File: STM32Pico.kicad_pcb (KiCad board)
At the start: 2 copper layers, 21.1 x 51.3 mm, 25 parts, among them J1 2.54mm header 01x20, J2 2.54mm header 01x20, SW1 Boot Mode, SW2 Reset Switch, U1 STM32F411CEUx, U2 XC6206PxxxMR, X1 ECS-2520MV-xxx-xx

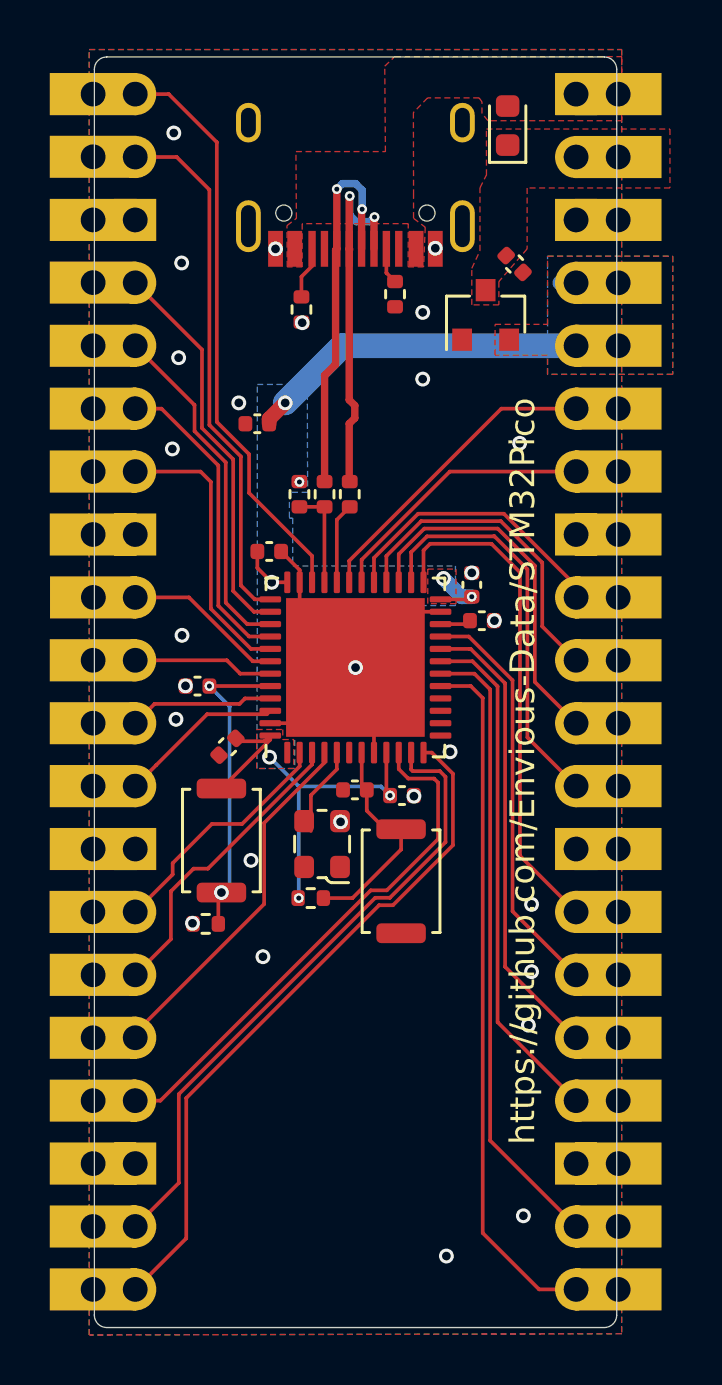
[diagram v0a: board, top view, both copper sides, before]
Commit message: added pin lables and Jtag/swdio/swclk on the PCB
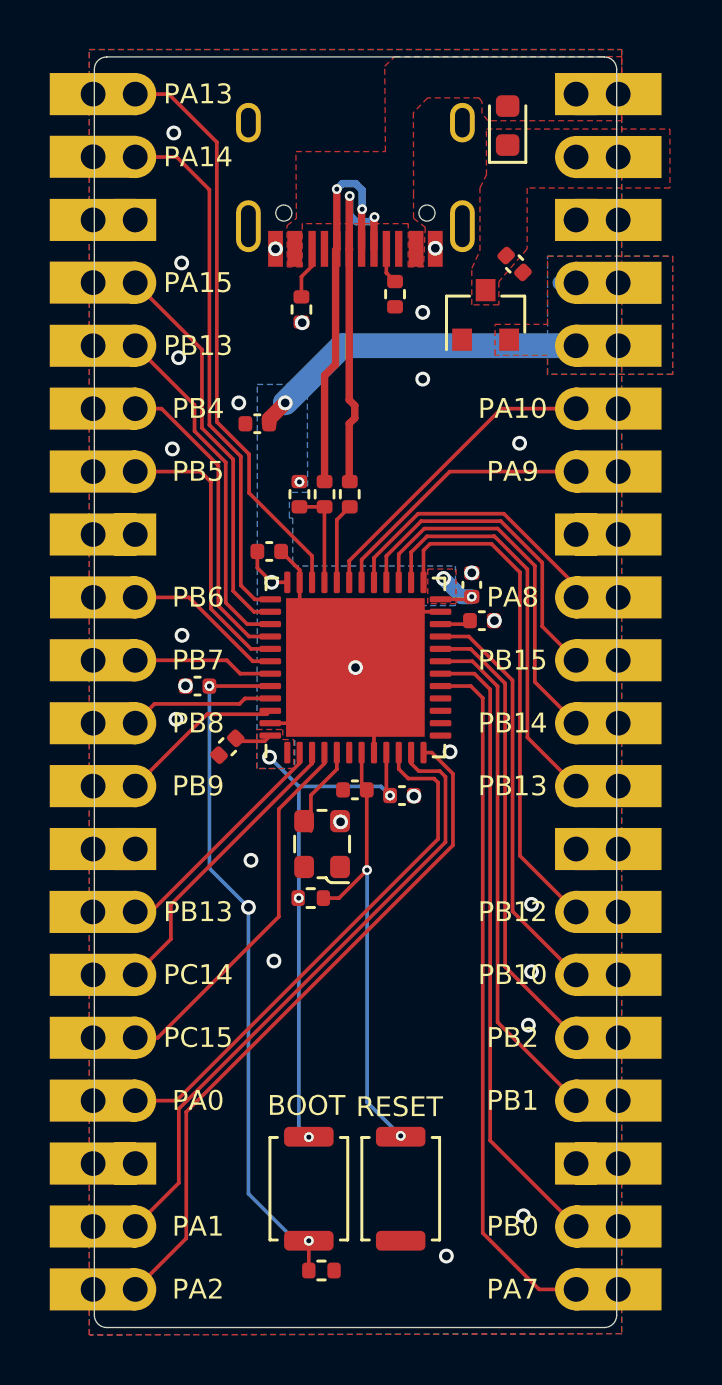
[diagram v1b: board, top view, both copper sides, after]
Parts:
- moved R7 14.8 mm to (102.3, 106.2), turned to 0 degrees
- moved SW1 14.5 mm to (101.8, 102.9)
- moved SW2 12.4 mm to (105.5, 102.9)
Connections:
- net PA13 renamed PA13-SWDIO
- net PA14 renamed PA14-SWCLK
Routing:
- net boot0: track 12.6 -> 28.0 mm, vias 2 -> 3
- net resetsw: track 8.91 -> 18.4 mm, vias 0 -> 2
- net +3V3: track 36.6 -> 43.4 mm, vias 8 -> 9
- net PC15: track 14.7 -> 15.2 mm
- net GND: vias 28 -> 27
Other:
- board text added: "BOOT"
- board text added: "JTCK"
- board text added: "JTDI"
- board text added: "JTMS"
- board text added: "PA0"
- board text added: "PA1"
- board text added: "PA10"
- board text added: "PA13"
- board text added: "PA14"
- board text added: "PA15"
- board text added: "PA2"
- board text added: "PA7"
- board text added: "PA8"
- board text added: "PA9"
- board text added: "PB0"
- board text added: "PB1"
- board text added: "PB10"
- board text added: "PB12"
- board text added: "PB13"
- board text added: "PB14"
- board text added: "PB15"
- board text added: "PB2"
- board text added: "PB4"
- board text added: "PB5"
- board text added: "PB6"
- board text added: "PB7"
- board text added: "PB8"
- board text added: "PB9"
- board text added: "PC14"
- board text added: "PC15"
- board text added: "RESET"
- board text added: "SWCLK"
- board text added: "SWDIO"
- board text removed: "https://github.com/Envious-Data/STM32Pico"

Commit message: changed diode for more common type
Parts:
- D1: value 1N4002 0603 -> 1N4002; footprint Diode_SMD:D_0603_1608Metric -> Diode_SMD:D_SOD-123

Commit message: adjusted pin labels
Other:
- board text added: "3V3"
- board text added: "VBUS"
- board text added: "VSYS"

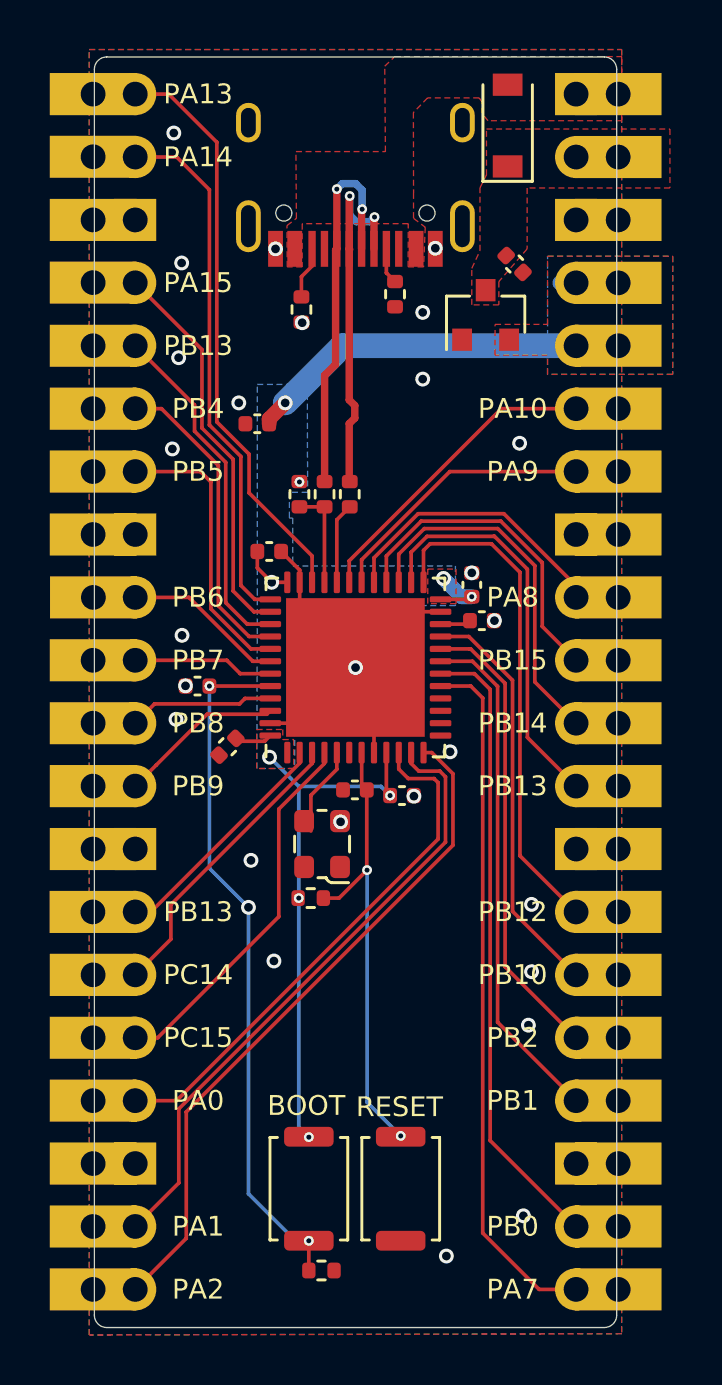
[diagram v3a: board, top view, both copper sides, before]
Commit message: swapped oscilator for crystal and adjusted various nearby parts and traces.
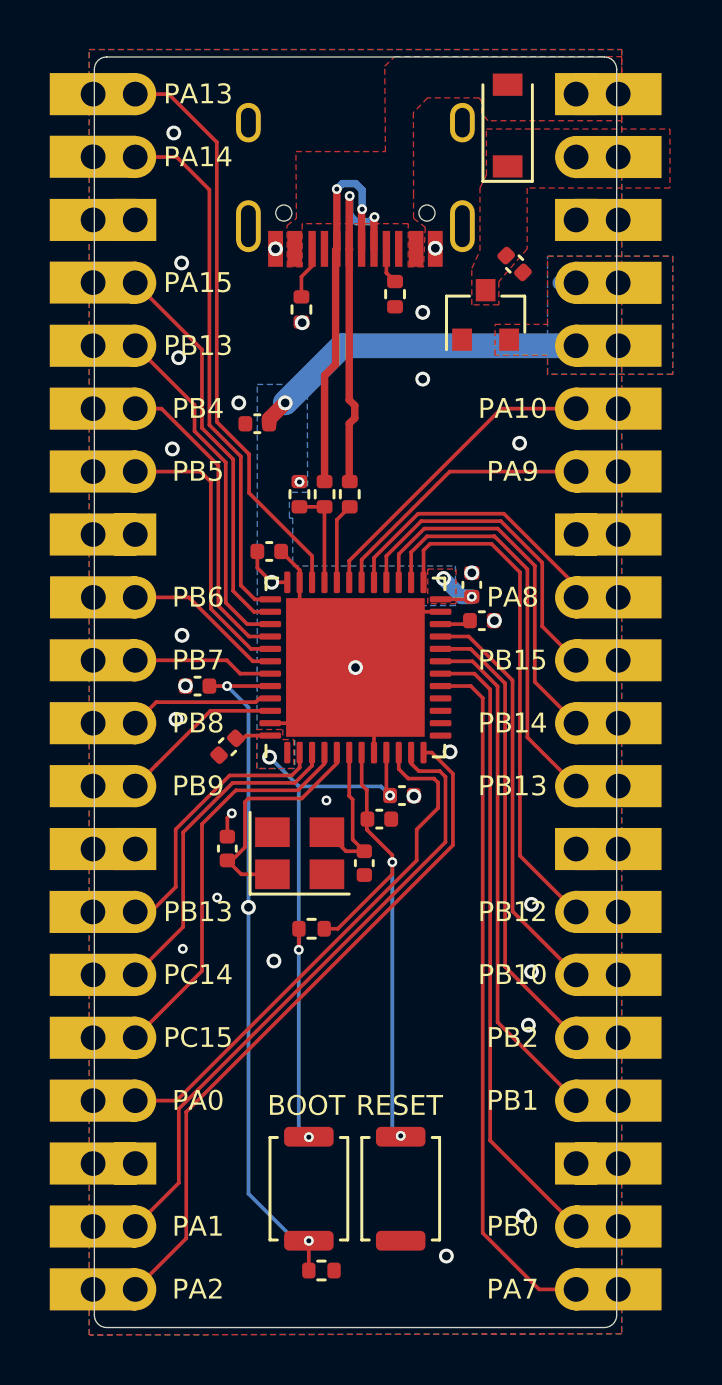
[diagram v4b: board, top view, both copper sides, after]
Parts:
- removed X1: ECS-2520MV-xxx-xx, Oscillator:Oscillator_SMD_ECS_2520MV-xxx-xx-4Pin_2.5x2.0mm
- added C10: 22pf capacitor, Capacitor_SMD:C_0402_1005Metric, F.Cu at (98.5, 89.2)
- added C11: 22pf capacitor, Capacitor_SMD:C_0402_1005Metric, F.Cu at (104.0, 89.8)
- added Y1: 8Mhz 3225, Crystal:Crystal_SMD_3225-4Pin_3.2x2.5mm, F.Cu at (101.4, 89.4)
- moved C9 1.54 mm to (104.6, 88.0), turned to 0 degrees
- moved R6 1.24 mm to (101.9, 92.4)
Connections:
- U1 pad 5: OSCpin -> OSCIN
- U1 pad 6: (no net) -> OSCOUT
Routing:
- net OSCIN: track 0.00 -> 9.60 mm
- net OSCOUT: track 0.00 -> 6.06 mm
- net OSCpin: track 3.60 -> 0.00 mm
- net resetsw: track 18.4 -> 20.3 mm
- net PC14: track 11.9 -> 13.4 mm
- net PC13: track 9.55 -> 11.0 mm
- net GND: track 18.4 -> 19.4 mm, vias 27 -> 29
- net PC15: track 15.2 -> 16.1 mm
- net +3V3: track 43.4 -> 44.3 mm

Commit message: added github url and fixed usb traces to not require vias
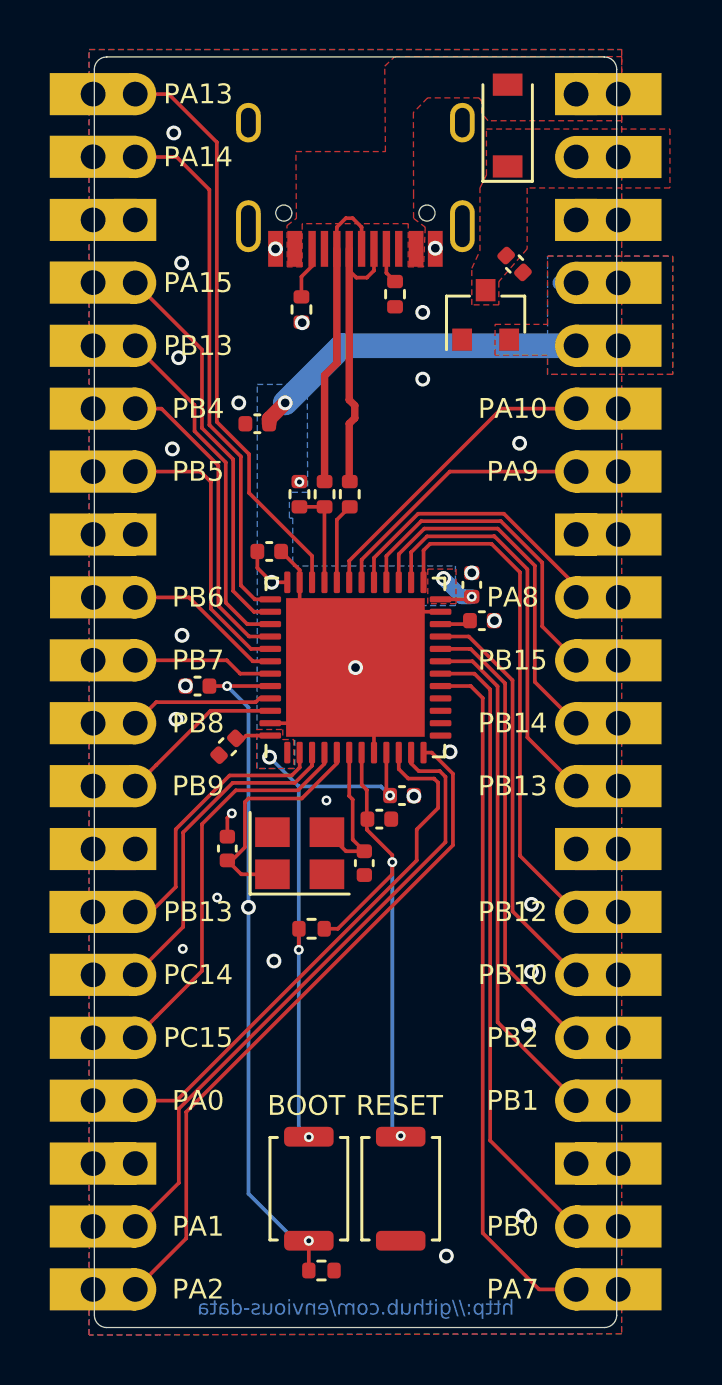
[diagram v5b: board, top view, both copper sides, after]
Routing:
- net D+: track 15.6 -> 12.7 mm, vias 2 -> 0
- net D-: track 15.0 -> 12.6 mm, vias 2 -> 0
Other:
- board text added: "http://github.com/envious-data"

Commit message: fixed some stuff and generated updated gerber
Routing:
- net +3V3: track 44.3 -> 47.5 mm
- net boot0: track 27.7 -> 30.4 mm
- net GND: vias 29 -> 27

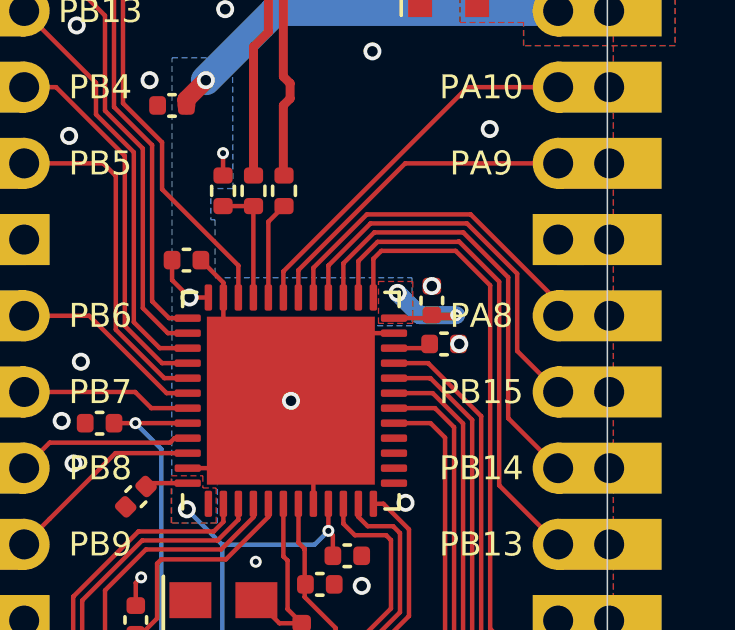
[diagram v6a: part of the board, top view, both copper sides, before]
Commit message: moved couple vias off pads
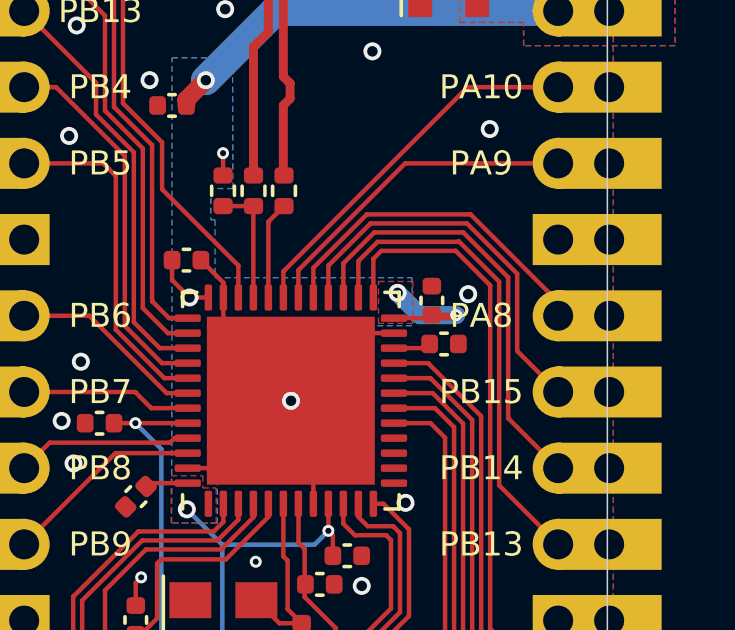
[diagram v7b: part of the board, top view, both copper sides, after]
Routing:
- net GND: vias 27 -> 26
